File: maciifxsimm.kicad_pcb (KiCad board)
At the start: 2 copper layers, 97.8 x 22.2 mm, 11 parts, among them J1 SIMM64_EDGE, U1 KM41C16000CK, U2 KM41C16000CK, U3 KM41C16000CK, U4 KM41C16000CK, U5 KM41C16000CK, U6 KM41C16000CK, U7 KM41C16000CK, U8 KM41C16000CK

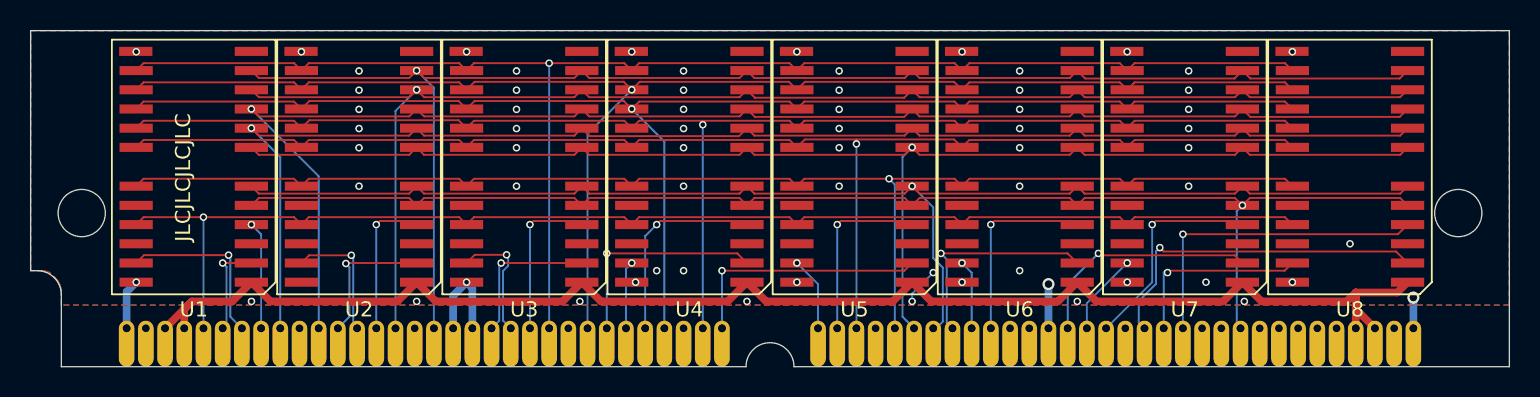
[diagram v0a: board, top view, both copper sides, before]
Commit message: fix issues found in the first run
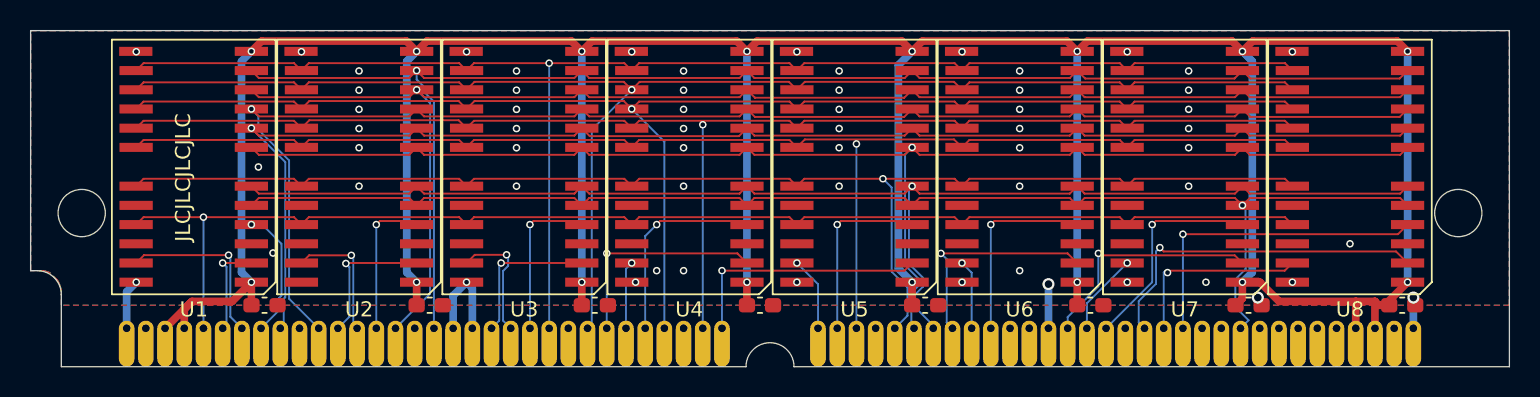
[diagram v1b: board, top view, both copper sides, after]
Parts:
- added C1: 100n, Capacitor_SMD:C_0603_1608Metric_Pad1.08x0.95mm_HandSolder, F.Cu at (119.0, 84.8)
- added C2: 100n, Capacitor_SMD:C_0603_1608Metric_Pad1.08x0.95mm_HandSolder, F.Cu at (129.9, 84.8)
- added C3: 100n, Capacitor_SMD:C_0603_1608Metric_Pad1.08x0.95mm_HandSolder, F.Cu at (140.8, 84.8)
- added C4: 100n, Capacitor_SMD:C_0603_1608Metric_Pad1.08x0.95mm_HandSolder, F.Cu at (151.7, 84.8)
- added C5: 100n, Capacitor_SMD:C_0603_1608Metric_Pad1.08x0.95mm_HandSolder, F.Cu at (162.7, 84.8)
- added C6: 100n, Capacitor_SMD:C_0603_1608Metric_Pad1.08x0.95mm_HandSolder, F.Cu at (173.6, 84.8)
- added C7: 100n, Capacitor_SMD:C_0603_1608Metric_Pad1.08x0.95mm_HandSolder, F.Cu at (184.0, 84.8)
- added C8: 100n, Capacitor_SMD:C_0603_1608Metric_Pad1.08x0.95mm_HandSolder, F.Cu at (194.2, 84.8)
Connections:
- J1 pad 3: VDD -> VCC
- J1 pad 4: VDD -> VCC
- J1 pad 61: VDD -> VCC
- J1 pad 62: VDD -> VCC
- U1 pad 1: VDD -> VCC
- U1 pad 12: (no net) -> VCC
- U2 pad 1: VDD -> VCC
- U2 pad 12: (no net) -> VCC
- U3 pad 1: VDD -> VCC
- U3 pad 12: (no net) -> VCC
- U4 pad 1: VDD -> VCC
- U4 pad 12: (no net) -> VCC
- U5 pad 1: VDD -> VCC
- U5 pad 12: (no net) -> VCC
- U6 pad 1: VDD -> VCC
- U6 pad 12: (no net) -> VCC
- U7 pad 1: VDD -> VCC
- U7 pad 12: (no net) -> VCC
- U8 pad 1: VDD -> VCC
- U8 pad 12: (no net) -> VCC
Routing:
- net VCC: track 0.00 -> 240.2 mm, vias 0 -> 16
- net VDD: track 97.8 -> 0.00 mm, vias 4 -> 0
- net GND: track 17.4 -> 14.9 mm, vias 71 -> 61
- net ~{W0}: track 7.12 -> 8.66 mm, vias 2 -> 1
- net A9: track 89.4 -> 90.2 mm, vias 2 -> 1
- net A2: track 95.7 -> 96.4 mm, vias 2 -> 1
- net ~{RAS}: track 87.7 -> 88.4 mm, vias 2 -> 1
- net A10: track 91.8 -> 92.1 mm, vias 2 -> 1
- net A0: track 93.4 -> 93.6 mm, vias 2 -> 1
- net A11: track 89.9 -> 90.2 mm, vias 2 -> 1
- net A7: vias 2 -> 1
- net ~{W7}: vias 2 -> 1
- net ~{W6}: vias 2 -> 1
- net ~{W5}: vias 2 -> 1
- net ~{W4}: vias 2 -> 1
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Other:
- board text added: "Macintosh IIfx 16 MB SIMM (v2) https://github.com/hanshuebner/maciifxsimm"
- board text removed: "Macintosh IIfx 16 MB SIMM (v1) https://github.com/hanshuebner/maciifxsimm"
